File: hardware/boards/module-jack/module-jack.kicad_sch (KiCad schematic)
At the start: 1 part, among them J7 2x10 2.54mm pin header

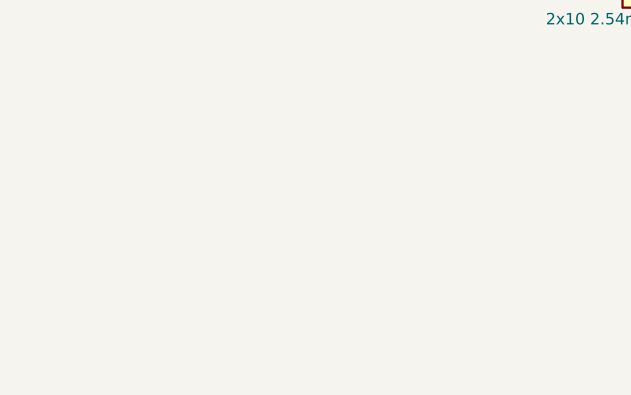
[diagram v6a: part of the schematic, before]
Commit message: module-jack: the four metal standoffs' pads on the sheet, on AGND_MOD (A7-9); export + render
MountingHole_Pad H1-H4, Row MECH-STANDOFF-MOD, Exclude from BOM, Assembly none.
The main board's pads are on no net, so they need no symbol: the layout places
them board-only, as the key boards' corner mounts are.

Co-Authored-By: Claude Opus 5.5 <noreply@anthropic.com>
Claude-Session: https://claude.ai/code/session_01LmB4muFXnoLprWX4JzuJ5A
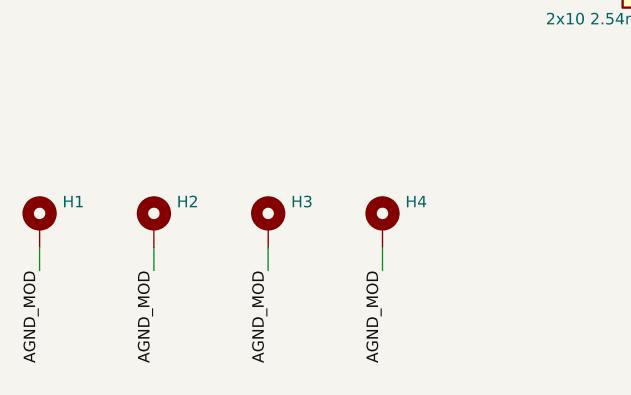
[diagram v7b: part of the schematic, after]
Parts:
- added H1, H2, H3, H4: M3 female-female hex spacer, MountingHole:MountingHole_3.2mm_M3_Pad, symbol Mechanical:MountingHole_Pad
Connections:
- net AGND_MOD: now also H1.1, H2.1, H3.1, H4.1
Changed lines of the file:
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@@
     (comment 4 "SOURCE - edit in KiCad 9; tools/kicad.py exports board-netlist.yaml")
   )
+  (symbol (lib_id "Mechanical:MountingHole_Pad") (at 40.64 101.60 0) (unit 1)
+    (in_bom no) (on_board yes) (dnp no)
+    (property "Reference" "H1" (at 43.18 99.06 0) (effects (font (size 1.27 1.27)) (justify left)))
+    (property "Value" "M3 female-female hex spacer" (at 43.18 96.52 0) (effects (font (size 1.27 1.27)) (justify left) hide))
+    (property "Footprint" "MountingHole:MountingHole_3.2mm_M3_Pad" (at 40.64 101.60 0) (effects (font (size 1.27 1.27)) hide))
+    (property "Datasheet" "" (at 40.64 101.60 0) (effects (font (size 1.27 1.27)) hide))
+    (property "Row" "MECH-STANDOFF-MOD" (at 40.64 101.60 0) (effects (font (size 1.27 1.27)) hide))
+    (property "Pins" "1=1" (at 40.64 101.60 0) (effects (font (size 1.27 1.27)) hide))
+    (property "Pins_source" "a mounting hole's one plated pad" (at 40.64 101.60 0) (effects (font (size 1.27 1.27)) hide))
+    (property "Note" "A metal standoff's pad (MECH-STANDOFF-MOD, owner 2026-09-30: metal). ON AGND_MOD on this board, and on NO NET on the main board, so the four make no second ground tie between the boards (dig-gnd-topology; power-entry.md, Grounding). Positions: config/module.yaml standoff.at. Plated, its pad under the standoff's face; nothing is bought for it here - the spacer is the BOM row" (at 40.64 101.60 0) (effects (font (size 1.27 1.27)) hide))
+    (property "Manufacturer" "" (at 40.64 101.60 0) (effects (font (size 1.27 1.27)) hide))
+    (property "MPN" "" (at 40.64 101.60 0) (effects (font (size 1.27 1.27)) hide))
+    (property "LCSC" "" (at 40.64 101.60 0) (effects (font (size 1.27 1.27)) hide))
+    (property "Assembly" "none" (at 40.64 101.60 0) (effects (font (size 1.27 1.27)) hide))
+    (pin "1")
+    (instances (project "module-jack" (path "/f69c67ba-c380-5393-90d5-6d2847e300fb" (reference "H1") (unit 1))))
+  )
+  (wire (pts (xy 40.64 104.14) (xy 40.64 106.68)) (stroke (width 0) (type default)))
+  (label "AGND_MOD" (at 40.64 106.68 270) (fields_autoplaced) (effects (font (size 1.27 1.27)) (justify right bottom)))
+  (symbol (lib_id "Mechanical:MountingHole_Pad") (at 53.34 101.60 0) (unit 1)
+    (in_bom no) (on_board yes) (dnp no)
+    (property "Reference" "H2" (at 55.88 99.06 0) (effects (font (size 1.27 1.27)) (justify left)))
+    (property "Value" "M3 female-female hex spacer" (at 55.88 96.52 0) (effects (font (size 1.27 1.27)) (justify left) hide))
+    (property "Footprint" "MountingHole:MountingHole_3.2mm_M3_Pad" (at 53.34 101.60 0) (effects (font (size 1.27 1.27)) hide))
+    (property "Datasheet" "" (at 53.34 101.60 0) (effects (font (size 1.27 1.27)) hide))
+    (property "Row" "MECH-STANDOFF-MOD" (at 53.34 101.60 0) (effects (font (size 1.27 1.27)) hide))
+    (property "Pins" "1=1" (at 53.34 101.60 0) (effects (font (size 1.27 1.27)) hide))
+    (property "Pins_source" "a mounting hole's one plated pad" (at 53.34 101.60 0) (effects (font (size 1.27 1.27)) hide))
+    (property "Note" "A metal standoff's pad (MECH-STANDOFF-MOD, owner 2026-09-30: metal). ON AGND_MOD on this board, and on NO NET on the main board, so the four make no second ground tie between the boards (dig-gnd-topology; power-entry.md, Grounding). Positions: config/module.yaml standoff.at. Plated, its pad under the standoff's face; nothing is bought for it here - the spacer is the BOM row" (at 53.34 101.60 0) (effects (font (size 1.27 1.27)) hide))
+    (property "Manufacturer" "" (at 53.34 101.60 0) (effects (font (size 1.27 1.27)) hide))
+    (property "MPN" "" (at 53.34 101.60 0) (effects (font (size 1.27 1.27)) hide))
+    (property "LCSC" "" (at 53.34 101.60 0) (effects (font (size 1.27 1.27)) hide))
+    (property "Assembly" "none" (at 53.34 101.60 0) (effects (font (size 1.27 1.27)) hide))
+    (pin "1")
+    (instances (project "module-jack" (path "/f69c67ba-c380-5393-90d5-6d2847e300fb" (reference "H2") (unit 1))))
+  )
+  (wire (pts (xy 53.34 104.14) (xy 53.34 106.68)) (stroke (width 0) (type default)))
+  (label "AGND_MOD" (at 53.34 106.68 270) (fields_autoplaced) (effects (font (size 1.27 1.27)) (justify right bottom)))
+  (symbol (lib_id "Mechanical:MountingHole_Pad") (at 66.04 101.60 0) (unit 1)
+    (in_bom no) (on_board yes) (dnp no)
+    (property "Reference" "H3" (at 68.58 99.06 0) (effects (font (size 1.27 1.27)) (justify left)))
+    (property "Value" "M3 female-female hex spacer" (at 68.58 96.52 0) (effects (font (size 1.27 1.27)) (justify left) hide))
+    (property "Footprint" "MountingHole:MountingHole_3.2mm_M3_Pad" (at 66.04 101.60 0) (effects (font (size 1.27 1.27)) hide))
+    (property "Datasheet" "" (at 66.04 101.60 0) (effects (font (size 1.27 1.27)) hide))
+    (property "Row" "MECH-STANDOFF-MOD" (at 66.04 101.60 0) (effects (font (size 1.27 1.27)) hide))
+    (property "Pins" "1=1" (at 66.04 101.60 0) (effects (font (size 1.27 1.27)) hide))
+    (property "Pins_source" "a mounting hole's one plated pad" (at 66.04 101.60 0) (effects (font (size 1.27 1.27)) hide))
+    (property "Note" "A metal standoff's pad (MECH-STANDOFF-MOD, owner 2026-09-30: metal). ON AGND_MOD on this board, and on NO NET on the main board, so the four make no second ground tie between the boards (dig-gnd-topology; power-entry.md, Grounding). Positions: config/module.yaml standoff.at. Plated, its pad under the standoff's face; nothing is bought for it here - the spacer is the BOM row" (at 66.04 101.60 0) (effects (font (size 1.27 1.27)) hide))
+    (property "Manufacturer" "" (at 66.04 101.60 0) (effects (font (size 1.27 1.27)) hide))
+    (property "MPN" "" (at 66.04 101.60 0) (effects (font (size 1.27 1.27)) hide))
+    (property "LCSC" "" (at 66.04 101.60 0) (effects (font (size 1.27 1.27)) hide))
+    (property "Assembly" "none" (at 66.04 101.60 0) (effects (font (size 1.27 1.27)) hide))
+    (pin "1")
+    (instances (project "module-jack" (path "/f69c67ba-c380-5393-90d5-6d2847e300fb" (reference "H3") (unit 1))))
+  )
+  (wire (pts (xy 66.04 104.14) (xy 66.04 106.68)) (stroke (width 0) (type default)))
+  (label "AGND_MOD" (at 66.04 106.68 270) (fields_autoplaced) (effects (font (size 1.27 1.27)) (justify right bottom)))
+  (symbol (lib_id "Mechanical:MountingHole_Pad") (at 78.74 101.60 0) (unit 1)
+    (in_bom no) (on_board yes) (dnp no)
+    (property "Reference" "H4" (at 81.28 99.06 0) (effects (font (size 1.27 1.27)) (justify left)))
+    (property "Value" "M3 female-female hex spacer" (at 81.28 96.52 0) (effects (font (size 1.27 1.27)) (justify left) hide))
+    (property "Footprint" "MountingHole:MountingHole_3.2mm_M3_Pad" (at 78.74 101.60 0) (effects (font (size 1.27 1.27)) hide))
+    (property "Datasheet" "" (at 78.74 101.60 0) (effects (font (size 1.27 1.27)) hide))
+    (property "Row" "MECH-STANDOFF-MOD" (at 78.74 101.60 0) (effects (font (size 1.27 1.27)) hide))
+    (property "Pins" "1=1" (at 78.74 101.60 0) (effects (font (size 1.27 1.27)) hide))
+    (property "Pins_source" "a mounting hole's one plated pad" (at 78.74 101.60 0) (effects (font (size 1.27 1.27)) hide))
+    (property "Note" "A metal standoff's pad (MECH-STANDOFF-MOD, owner 2026-09-30: metal). ON AGND_MOD on this board, and on NO NET on the main board, so the four make no second ground tie between the boards (dig-gnd-topology; power-entry.md, Grounding). Positions: config/module.yaml standoff.at. Plated, its pad under the standoff's face; nothing is bought for it here - the spacer is the BOM row" (at 78.74 101.60 0) (effects (font (size 1.27 1.27)) hide))
+    (property "Manufacturer" "" (at 78.74 101.60 0) (effects (font (size 1.27 1.27)) hide))
+    (property "MPN" "" (at 78.74 101.60 0) (effects (font (size 1.27 1.27)) hide))
+    (property "LCSC" "" (at 78.74 101.60 0) (effects (font (size 1.27 1.27)) hide))
+    (property "Assembly" "none" (at 78.74 101.60 0) (effects (font (size 1.27 1.27)) hide))
+    (pin "1")
+    (instances (project "module-jack" (path "/f69c67ba-c380-5393-90d5-6d2847e300fb" (reference "H4") (unit 1))))
+  )
+  (wire (pts (xy 78.74 104.14) (xy 78.74 106.68)) (stroke (width 0) (type default)))
+  (label "AGND_MOD" (at 78.74 106.68 270) (fields_autoplaced) (effects (font (size 1.27 1.27)) (justify right bottom)))
   (symbol (lib_id "Connector_Generic:Conn_02x10_Odd_Even") (at 106.68 63.5 0) (unit 1)
     (in_bom yes) (on_board yes) (dnp no)

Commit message: LED-PANEL moves to the main board (LTST-C171GKT under a Bivar PLP2-750 light pipe); J-B2B-MOD pin 19 freed; jack board keeps H1-H2; panel standoffs and studs in the BOM
Co-Authored-By: Claude Opus 5.5 <noreply@anthropic.com>
Claude-Session: https://claude.ai/code/session_01LmB4muFXnoLprWX4JzuJ5A
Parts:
- removed H3, H4: M3 female-female hex spacer, MountingHole:MountingHole_3.2mm_M3_Pad, symbol Mechanical:MountingHole_Pad
- H1, H2: Note A metal standoff's pad (MECH-STANDOFF-MOD, owner 2026-09-30: metal). ON AGND_MOD on this board, and on NO NET on the main board, so the four make no second ground tie between the boards (dig-gnd-topology; power-entry.md, Grounding). Positions: config/module.yaml standoff.at. Plated, its pad under the standoff's face; nothing is bought for it here - the spacer is the BOM row -> A metal standoff's pad (MECH-STANDOFF-MOD, owner 2026-09-30: metal). ON AGND_MOD on this board, and on NO NET on the main board, so the two make no second ground tie between the boards (dig-gnd-topology; power-entry.md, Grounding). Positions: config/module.yaml standoff.at - the two above the pots; the jack board has no low standoffs since it became a plain rectangle (ADR 0024 point 15). Plated, its pad under the standoff's face; nothing is bought for it here - the spacer is the BOM row
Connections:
- net UMBILICAL_POS12: no longer names the net of J7.19 (Pin_19)
- no-connect marks 0 -> 1
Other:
- removed sheet panel-led
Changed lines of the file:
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@@
     (property "Pins" "1=1" (at 40.64 101.60 0) (effects (font (size 1.27 1.27)) hide))
     (property "Pins_source" "a mounting hole's one plated pad" (at 40.64 101.60 0) (effects (font (size 1.27 1.27)) hide))
-    (property "Note" "A metal standoff's pad (MECH-STANDOFF-MOD, owner 2026-09-30: metal). ON AGND_MOD on this board, and on NO NET on the main board, so the four make no second ground tie between the boards (dig-gnd-topology; power-entry.md, Grounding). Positions: config/module.yaml standoff.at. Plated, its pad under the standoff's face; nothing is bought for it here - the spacer is the BOM row" (at 40.64 101.60 0) (effects (font (size 1.27 1.27)) hide))
+    (property "Note" "A metal standoff's pad (MECH-STANDOFF-MOD, owner 2026-09-30: metal). ON AGND_MOD on this board, and on NO NET on the main board, so the two make no second ground tie between the boards (dig-gnd-topology; power-entry.md, Grounding). Positions: config/module.yaml standoff.at - the two above the pots; the jack board has no low standoffs since it became a plain rectangle (ADR 0024 point 15). Plated, its pad under the standoff's face; nothing is bought for it here - the spacer is the BOM row" (at 40.64 101.60 0) (effects (font (size 1.27 1.27)) hide))
     (property "Manufacturer" "" (at 40.64 101.60 0) (effects (font (size 1.27 1.27)) hide))
     (property "MPN" "" (at 40.64 101.60 0) (effects (font (size 1.27 1.27)) hide))
@@
     (property "Pins" "1=1" (at 53.34 101.60 0) (effects (font (size 1.27 1.27)) hide))
     (property "Pins_source" "a mounting hole's one plated pad" (at 53.34 101.60 0) (effects (font (size 1.27 1.27)) hide))
-    (property "Note" "A metal standoff's pad (MECH-STANDOFF-MOD, owner 2026-09-30: metal). ON AGND_MOD on this board, and on NO NET on the main board, so the four make no second ground tie between the boards (dig-gnd-topology; power-entry.md, Grounding). Positions: config/module.yaml standoff.at. Plated, its pad under the standoff's face; nothing is bought for it here - the spacer is the BOM row" (at 53.34 101.60 0) (effects (font (size 1.27 1.27)) hide))
+    (property "Note" "A metal standoff's pad (MECH-STANDOFF-MOD, owner 2026-09-30: metal). ON AGND_MOD on this board, and on NO NET on the main board, so the two make no second ground tie between the boards (dig-gnd-topology; power-entry.md, Grounding). Positions: config/module.yaml standoff.at - the two above the pots; the jack board has no low standoffs since it became a plain rectangle (ADR 0024 point 15). Plated, its pad under the standoff's face; nothing is bought for it here - the spacer is the BOM row" (at 53.34 101.60 0) (effects (font (size 1.27 1.27)) hide))
     (property "Manufacturer" "" (at 53.34 101.60 0) (effects (font (size 1.27 1.27)) hide))
     (property "MPN" "" (at 53.34 101.60 0) (effects (font (size 1.27 1.27)) hide))
@@
   (wire (pts (xy 53.34 104.14) (xy 53.34 106.68)) (stroke (width 0) (type default)))
   (label "AGND_MOD" (at 53.34 106.68 270) (fields_autoplaced) (effects (font (size 1.27 1.27)) (justify right bottom)))
-  (symbol (lib_id "Mechanical:MountingHole_Pad") (at 66.04 101.60 0) (unit 1)
-    (in_bom no) (on_board yes) (dnp no)
-    (property "Reference" "H3" (at 68.58 99.06 0) (effects (font (size 1.27 1.27)) (justify left)))
-    (property "Value" "M3 female-female hex spacer" (at 68.58 96.52 0) (effects (font (size 1.27 1.27)) (justify left) hide))
-    (property "Footprint" "MountingHole:MountingHole_3.2mm_M3_Pad" (at 66.04 101.60 0) (effects (font (size 1.27 1.27)) hide))
-    (property "Datasheet" "" (at 66.04 101.60 0) (effects (font (size 1.27 1.27)) hide))
-    (property "Row" "MECH-STANDOFF-MOD" (at 66.04 101.60 0) (effects (font (size 1.27 1.27)) hide))
-    (property "Pins" "1=1" (at 66.04 101.60 0) (effects (font (size 1.27 1.27)) hide))
-    (property "Pins_source" "a mounting hole's one plated pad" (at 66.04 101.60 0) (effects (font (size 1.27 1.27)) hide))
-    (property "Note" "A metal standoff's pad (MECH-STANDOFF-MOD, owner 2026-09-30: metal). ON AGND_MOD on this board, and on NO NET on the main board, so the four make no second ground tie between the boards (dig-gnd-topology; power-entry.md, Grounding). Positions: config/module.yaml standoff.at. Plated, its pad under the standoff's face; nothing is bought for it here - the spacer is the BOM row" (at 66.04 101.60 0) (effects (font (size 1.27 1.27)) hide))
-    (property "Manufacturer" "" (at 66.04 101.60 0) (effects (font (size 1.27 1.27)) hide))
-    (property "MPN" "" (at 66.04 101.60 0) (effects (font (size 1.27 1.27)) hide))
-    (property "LCSC" "" (at 66.04 101.60 0) (effects (font (size 1.27 1.27)) hide))
-    (property "Assembly" "none" (at 66.04 101.60 0) (effects (font (size 1.27 1.27)) hide))
-    (pin "1")
-    (instances (project "module-jack" (path "/f69c67ba-c380-5393-90d5-6d2847e300fb" (reference "H3") (unit 1))))
-  )
-  (wire (pts (xy 66.04 104.14) (xy 66.04 106.68)) (stroke (width 0) (type default)))
-  (label "AGND_MOD" (at 66.04 106.68 270) (fields_autoplaced) (effects (font (size 1.27 1.27)) (justify right bottom)))
-  (symbol (lib_id "Mechanical:MountingHole_Pad") (at 78.74 101.60 0) (unit 1)
-    (in_bom no) (on_board yes) (dnp no)
-    (property "Reference" "H4" (at 81.28 99.06 0) (effects (font (size 1.27 1.27)) (justify left)))
-    (property "Value" "M3 female-female hex spacer" (at 81.28 96.52 0) (effects (font (size 1.27 1.27)) (justify left) hide))
-    (property "Footprint" "MountingHole:MountingHole_3.2mm_M3_Pad" (at 78.74 101.60 0) (effects (font (size 1.27 1.27)) hide))
-    (property "Datasheet" "" (at 78.74 101.60 0) (effects (font (size 1.27 1.27)) hide))
-    (property "Row" "MECH-STANDOFF-MOD" (at 78.74 101.60 0) (effects (font (size 1.27 1.27)) hide))
-    (property "Pins" "1=1" (at 78.74 101.60 0) (effects (font (size 1.27 1.27)) hide))
-    (property "Pins_source" "a mounting hole's one plated pad" (at 78.74 101.60 0) (effects (font (size 1.27 1.27)) hide))
-    (property "Note" "A metal standoff's pad (MECH-STANDOFF-MOD, owner 2026-09-30: metal). ON AGND_MOD on this board, and on NO NET on the main board, so the four make no second ground tie between the boards (dig-gnd-topology; power-entry.md, Grounding). Positions: config/module.yaml standoff.at. Plated, its pad under the standoff's face; nothing is bought for it here - the spacer is the BOM row" (at 78.74 101.60 0) (effects (font (size 1.27 1.27)) hide))
-    (property "Manufacturer" "" (at 78.74 101.60 0) (effects (font (size 1.27 1.27)) hide))
-    (property "MPN" "" (at 78.74 101.60 0) (effects (font (size 1.27 1.27)) hide))
-    (property "LCSC" "" (at 78.74 101.60 0) (effects (font (size 1.27 1.27)) hide))
-    (property "Assembly" "none" (at 78.74 101.60 0) (effects (font (size 1.27 1.27)) hide))
-    (pin "1")
-    (instances (project "module-jack" (path "/f69c67ba-c380-5393-90d5-6d2847e300fb" (reference "H4") (unit 1))))
-  )
-  (wire (pts (xy 78.74 104.14) (xy 78.74 106.68)) (stroke (width 0) (type default)))
-  (label "AGND_MOD" (at 78.74 106.68 270) (fields_autoplaced) (effects (font (size 1.27 1.27)) (justify right bottom)))
   (symbol (lib_id "Connector_Generic:Conn_02x10_Odd_Even") (at 106.68 63.5 0) (unit 1)
     (in_bom yes) (on_board yes) (dnp no)
@@
   (wire (pts (xy 203.2 99.06) (xy 200.66 99.06)) (stroke (width 0) (type default)))
   (label "AGND_MOD" (at 200.66 99.06 180) (fields_autoplaced) (effects (font (size 1.27 1.27)) (justify right bottom)))
-  (wire (pts (xy 457.2 93.98) (xy 454.66 93.98)) (stroke (width 0) (type default)))
-  (label "AGND_MOD" (at 454.66 93.98 180) (fields_autoplaced) (effects (font (size 1.27 1.27)) (justify right bottom)))
   (wire (pts (xy 101.6 55.88) (xy 99.06 55.88)) (stroke (width 0) (type default)))
   (label "GAIN_WIPER" (at 99.06 55.88 180) (fields_autoplaced) (effects (font (size 1.27 1.27)) (justify right bottom)))
@@
   (wire (pts (xy 203.2 93.98) (xy 200.66 93.98)) (stroke (width 0) (type default)))
   (label "MOD3_JACK" (at 200.66 93.98 180) (fields_autoplaced) (effects (font (size 1.27 1.27)) (justify right bottom)))
-  (wire (pts (xy 101.6 76.2) (xy 99.06 76.2)) (stroke (width 0) (type default)))
-  (label "UMBILICAL_POS12" (at 99.06 76.2 180) (fields_autoplaced) (effects (font (size 1.27 1.27)) (justify right bottom)))
-  (wire (pts (xy 457.2 91.44) (xy 454.66 91.44)) (stroke (width 0) (type default)))
-  (label "UMBILICAL_POS12" (at 454.66 91.44 180) (fields_autoplaced) (effects (font (size 1.27 1.27)) (justify right bottom)))
   (wire (pts (xy 114.3 76.2) (xy 116.84 76.2)) (stroke (width 0) (type default)))
   (label "MOD4_JACK" (at 116.84 76.2 0) (fields_autoplaced) (effects (font (size 1.27 1.27)) (justify left bottom)))
@@
     (instances (project "module-jack" (path "/f69c67ba-c380-5393-90d5-6d2847e300fb" (page "5"))))
   )
-  (sheet (at 457.2 88.9) (size 50.8 10.16) (exclude_from_sim no) (in_bom yes) (on_board yes) (dnp no)
-    (stroke (width 0.1524) (type solid)) (fill (color 0 0 0 0.0000))
-    (property "Sheetname" "panel-led" (at 457.2 87.63 0) (effects (font (size 1.27 1.27)) (justify left bottom)))
-    (property "Sheetfile" "../../module/panel-led/panel-led.kicad_sch" (at 457.2 99.06 0) (effects (font (size 1.27 1.27)) (justify left top)))
-    (pin "UMBILICAL_POS12" input (at 457.2 91.44 180) (effects (font (size 1.27 1.27)) (justify left)))
-    (pin "AGND_MOD" passive (at 457.2 93.98 180) (effects (font (size 1.27 1.27)) (justify left)))
-    (instances (project "module-jack" (path "/f69c67ba-c380-5393-90d5-6d2847e300fb" (page "6"))))
-  )
+  (no_connect (at 101.6 76.2))
   (sheet_instances (path "/" (page "1")))
 )
